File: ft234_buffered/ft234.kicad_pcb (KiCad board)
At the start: 2 copper layers, 17.5 x 10.2 mm, 16 parts, among them J1 USB_OTG, J2 Conn_01x04, U1 FT234XD, U2 74LVC1G17, U3 74LVC1G17

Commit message: migrate to KiCad 7
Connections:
- C1 pad 1: Net-(C1-Pad1) -> (no net)
- C2 pad 1: Net-(C2-Pad1) -> (no net)
- D1 pad 1: Net-(D1-Pad1) -> (no net)
- J1 pad 2: Net-(C1-Pad1) -> Net-(J1-D-)
- J1 pad 3: Net-(C2-Pad1) -> Net-(J1-D+)
- R1 pad 1: Net-(R1-Pad1) -> (no net)
- R1 pad 2: Net-(C1-Pad1) -> Net-(J1-D-)
- R2 pad 1: Net-(R2-Pad1) -> (no net)
- R2 pad 2: Net-(C2-Pad1) -> Net-(J1-D+)
- R4 pad 1: Net-(D1-Pad1) -> Net-(D1-K)
- R4 pad 2: Net-(R4-Pad2) -> (no net)
- U1 pad 1: Net-(R1-Pad1) -> Net-(U1-USBDM)
- U1 pad 10: Net-(U1-Pad10) -> (no net)
- U1 pad 12: Net-(R2-Pad1) -> Net-(U1-UDBDP)
- U1 pad 6: Net-(R4-Pad2) -> Net-(U1-CBUS0)
- U1 pad 7: Net-(U1-Pad7) -> (no net)
- U2 pad 2: Net-(U1-Pad7) -> Net-(U1-TXD)
- U3 pad 4: Net-(U1-Pad10) -> Net-(U1-RXD)
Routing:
- net Net-(U1-TXD): track 0.00 -> 6.06 mm, vias 0 -> 2
- net Net-(U1-Pad7): track 6.06 -> 0.00 mm, vias 2 -> 0
- net Net-(U1-RXD): track 0.00 -> 5.21 mm
- net Net-(U1-Pad10): track 5.21 -> 0.00 mm
- net Net-(J1-D-): track 0.00 -> 4.70 mm
- net Net-(C1-Pad1): track 4.70 -> 0.00 mm
- net Net-(U1-CBUS0): track 0.00 -> 3.44 mm
- net Net-(R4-Pad2): track 3.44 -> 0.00 mm
- net Net-(J1-D+): track 0.00 -> 2.83 mm
- net Net-(C2-Pad1): track 2.83 -> 0.00 mm
- net Net-(D1-Pad1): track 0.99 -> 0.00 mm
- net Net-(D1-K): track 0.00 -> 0.99 mm
- net Net-(U1-UDBDP): track 0.00 -> 0.94 mm
- net Net-(R2-Pad1): track 0.94 -> 0.00 mm
- net Net-(U1-USBDM): track 0.00 -> 0.94 mm
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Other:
- net class Default removed

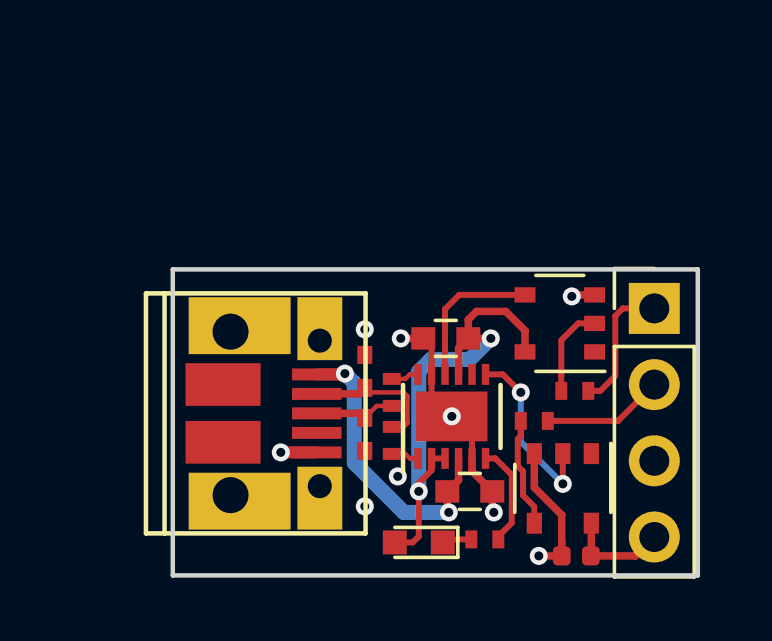
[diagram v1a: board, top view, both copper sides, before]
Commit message: changing buffered ft234 board - wip
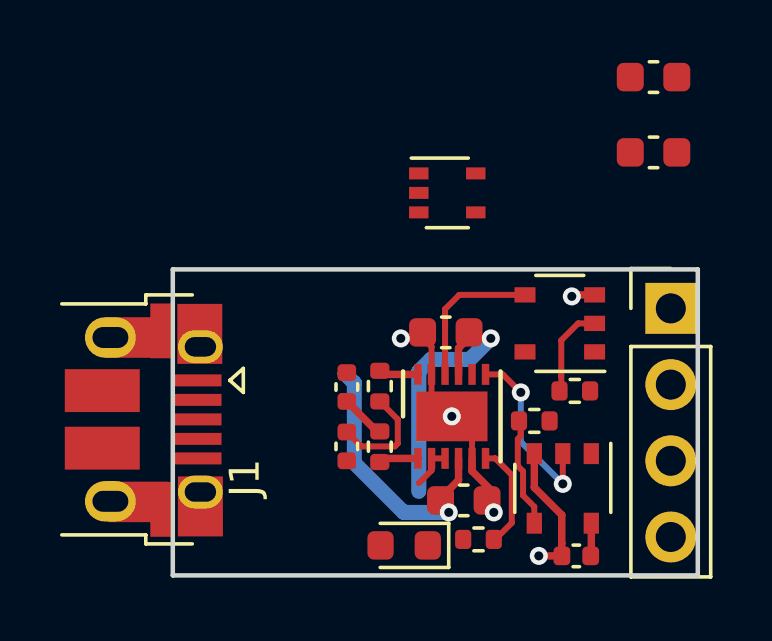
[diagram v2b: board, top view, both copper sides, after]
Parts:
- added C5: 4.7u/6.3V, Capacitor_SMD:C_0603_1608Metric, F.Cu at (156.0, 63.6)
- added C7: 4.7u/6.3V, Capacitor_SMD:C_0603_1608Metric, F.Cu at (156.0, 66.1)
- added U4: MIC5365-2.5YC5, Package_TO_SOT_SMD:SOT-353_SC-70-5, F.Cu at (149.2, 67.5)
- C1, C2: footprint Capacitors_SMD:C_0402_NoSilk -> Capacitor_SMD:C_0402_1005Metric
- C3, C4: footprint Capacitors_SMD:C_0603 -> Capacitor_SMD:C_0603_1608Metric
- D1: footprint LEDs:LED_0603 -> LED_SMD:LED_0603_1608Metric
- J1: footprint hunz:USB_Micro-B_10103594-0001LF -> Connector_USB:USB_Micro-B_Amphenol_10103594-0001LF_Horizontal
- R1, R2, R3, R4, R5: footprint Resistors_SMD:R_0402_NoSilk -> Resistor_SMD:R_0402_1005Metric
- U1: footprint Housings_DFN_QFN:DFN-12-1EP_3x3mm_Pitch0.45mm -> Package_DFN_QFN:DFN-12-1EP_3x3mm_P0.45mm_EP1.66x2.38mm
- moved J1 3.77 mm to (139.0, 75.0), turned to -90 degrees
- moved C1 0.79 mm to (145.8, 73.9)
- moved C2 0.72 mm to (145.8, 75.9)
- moved J2 0.55 mm to (156.6, 71.3)
- moved D1 0.50 mm to (147.7, 79.2)
- moved R1 0.45 mm to (146.9, 75.9)
- moved R2 0.45 mm to (146.9, 73.9)
- moved C4 0.36 mm to (149.7, 77.7)
- moved R4 0.21 mm to (150.2, 79.0)
- moved C3 0.20 mm to (149.1, 72.1)
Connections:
- C1 pad 1: (no net) -> Net-(J1-D-)
- C2 pad 1: (no net) -> Net-(J1-D+)
- D1 pad 1: (no net) -> Net-(D1-K)
- J1 pad 4: (no net) -> unconnected-(J1-ID-Pad4)
- R1 pad 1: (no net) -> Net-(U1-USBDM)
- R2 pad 1: (no net) -> Net-(U1-UDBDP)
- R4 pad 2: (no net) -> Net-(U1-CBUS0)
- U1 pad 10: (no net) -> Net-(U1-RXD)
- U1 pad 7: (no net) -> Net-(U1-TXD)
- U1 pad 8: (no net) -> unconnected-(U1-~{RTS}-Pad8)
- U3 pad 5: +3V3 -> +2V5
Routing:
- net +3V3: track 16.7 -> 10.4 mm, vias 2 -> 1
- net /RXIN: track 4.51 -> 0.00 mm
- net /TXOUT: track 4.05 -> 0.00 mm
- net Net-(J1-D-): track 4.70 -> 1.51 mm
- net /VTG: track 3.47 -> 1.10 mm
- net GND: track 12.7 -> 11.5 mm, vias 9 -> 5
- net Net-(D1-K): track 0.99 -> 0.00 mm
- net +5V: track 9.86 -> 8.92 mm, vias 2 -> 1
- net Net-(J1-D+): track 2.83 -> 3.59 mm

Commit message: foo
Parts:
- moved C7 9.43 mm to (146.7, 67.5), turned to -90 degrees
- moved C5 5.90 mm to (151.6, 67.5), turned to -90 degrees
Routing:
- net GND: track 11.5 -> 10.8 mm, vias 5 -> 4
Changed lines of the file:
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@@
   )
   (footprint "Capacitor_SMD:C_0603_1608Metric" (layer "F.Cu")
-    (at 156.025 63.59)
+    (at 151.6 67.5 -90)
     (descr "Capacitor SMD 0603 (1608 Metric), square (rectangular) end terminal, IPC_7351 nominal, (Body size source: IPC-SM-782 page 76, https://www.pcb-3d.com/wordpress/wp-content/uploads/ipc-sm-782a_amendment_1_and_2.pdf), generated with kicad-footprint-generator")
     (tags "capacitor")
@@
     (property "ki_keywords" "cap capacitor")
     (attr smd)
-    (fp_text reference "C5" (at 0 -1.43) (layer "F.SilkS") hide
+    (fp_text reference "C5" (at 0 -1.43 90) (layer "F.SilkS") hide
         (effects (font (size 1 1) (thickness 0.15)))
     )
-    (fp_text value "4.7u/6.3V" (at 0 1.43) (layer "F.Fab")
+    (fp_text value "4.7u/6.3V" (at 0 1.43 90) (layer "F.Fab")
         (effects (font (size 1 1) (thickness 0.15)))
     )
-    (fp_text user "${REFERENCE}" (at 0 0) (layer "F.Fab")
+    (fp_text user "${REFERENCE}" (at 0 0 90) (layer "F.Fab")
         (effects (font (size 0.4 0.4) (thickness 0.06)))
     )
@@
     (fp_line (start 0.8 0.4) (end -0.8 0.4)
       (stroke (width 0.1) (type solid)) (layer "F.Fab"))
-    (pad "1" smd roundrect (at -0.775 0) (size 0.9 0.95) (layers "F.Cu" "F.Paste" "F.Mask") (roundrect_rratio 0.25)
+    (pad "1" smd roundrect (at -0.775 0 270) (size 0.9 0.95) (layers "F.Cu" "F.Paste" "F.Mask") (roundrect_rratio 0.25)
       (net 19 "+2V5") (pintype "passive"))
-    (pad "2" smd roundrect (at 0.775 0) (size 0.9 0.95) (layers "F.Cu" "F.Paste" "F.Mask") (roundrect_rratio 0.25)
+    (pad "2" smd roundrect (at 0.775 0 270) (size 0.9 0.95) (layers "F.Cu" "F.Paste" "F.Mask") (roundrect_rratio 0.25)
       (net 1 "GND") (pintype "passive"))
     (model "${KICAD6_3DMODEL_DIR}/Capacitor_SMD.3dshapes/C_0603_1608Metric.wrl"
@@
   )
   (footprint "Capacitor_SMD:C_0603_1608Metric" (layer "F.Cu")
-    (at 156.025 66.1)
+    (at 146.7 67.5 -90)
     (descr "Capacitor SMD 0603 (1608 Metric), square (rectangular) end terminal, IPC_7351 nominal, (Body size source: IPC-SM-782 page 76, https://www.pcb-3d.com/wordpress/wp-content/uploads/ipc-sm-782a_amendment_1_and_2.pdf), generated with kicad-footprint-generator")
     (tags "capacitor")
@@
     (property "ki_keywords" "cap capacitor")
     (attr smd)
-    (fp_text reference "C7" (at 0 -1.43) (layer "F.SilkS") hide
+    (fp_text reference "C7" (at 0 -1.43 90) (layer "F.SilkS") hide
         (effects (font (size 1 1) (thickness 0.15)))
     )
-    (fp_text value "4.7u/6.3V" (at 0 1.43) (layer "F.Fab")
+    (fp_text value "4.7u/6.3V" (at 0 1.43 90) (layer "F.Fab")
         (effects (font (size 1 1) (thickness 0.15)))
     )
-    (fp_text user "${REFERENCE}" (at 0 0) (layer "F.Fab")
+    (fp_text user "${REFERENCE}" (at 0 0 90) (layer "F.Fab")
         (effects (font (size 0.4 0.4) (thickness 0.06)))
     )
@@
     (fp_line (start 0.8 0.4) (end -0.8 0.4)
       (stroke (width 0.1) (type solid)) (layer "F.Fab"))
-    (pad "1" smd roundrect (at -0.775 0) (size 0.9 0.95) (layers "F.Cu" "F.Paste" "F.Mask") (roundrect_rratio 0.25)
+    (pad "1" smd roundrect (at -0.775 0 270) (size 0.9 0.95) (layers "F.Cu" "F.Paste" "F.Mask") (roundrect_rratio 0.25)
       (net 5 "+5V") (pintype "passive"))
-    (pad "2" smd roundrect (at 0.775 0) (size 0.9 0.95) (layers "F.Cu" "F.Paste" "F.Mask") (roundrect_rratio 0.25)
+    (pad "2" smd roundrect (at 0.775 0 270) (size 0.9 0.95) (layers "F.Cu" "F.Paste" "F.Mask") (roundrect_rratio 0.25)
       (net 1 "GND") (pintype "passive"))
     (model "${KICAD6_3DMODEL_DIR}/Capacitor_SMD.3dshapes/C_0603_1608Metric.wrl"
@@
   (segment (start 150.65 77.4) (end 150.65 78.05) (width 0.25) (layer "F.Cu") (net 1))
   (segment (start 148.625 74.405) (end 148.705 74.485) (width 0.2) (layer "F.Cu") (net 1))
-  (segment (start 148.35 72.3) (end 147.6 72.3) (width 0.25) (layer "F.Cu") (net 1))
   (segment (start 149.975 76.3) (end 149.975 76.725) (width 0.25) (layer "F.Cu") (net 1))
   (segment (start 152.965 79.55) (end 152.2 79.55) (width 0.25) (layer "F.Cu") (net 1))
@@
   (segment (start 154.06 70.85) (end 153.35 70.85) (width 0.25) (layer "F.Cu") (net 1))
   (via (at 149.3 74.9) (size 0.6) (drill 0.3) (layers "F.Cu" "B.Cu") (net 1))
-  (via (at 147.6 72.3) (size 0.6) (drill 0.3) (layers "F.Cu" "B.Cu") (net 1))
   (via (at 152.2 79.55) (size 0.6) (drill 0.3) (layers "F.Cu" "B.Cu") (net 1))
   (via (at 153.3 70.9) (size 0.6) (drill 0.3) (layers "F.Cu" "B.Cu") (net 1))

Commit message: wip
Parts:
- C3, C4, C5, C7: footprint Capacitor_SMD:C_0603_1608Metric -> Capacitor_SMD:C_0402_1005Metric
- moved U4 4.83 mm to (146.4, 71.5)
- moved C7 4.39 mm to (143.8, 70.8), turned to 180 degrees
- moved C5 4.06 mm to (149.1, 70.7), turned to 0 degrees
- moved J1 2.90 mm to (141.8, 75.8)
- moved D1 0.95 mm to (147.2, 78.4), turned to 90 degrees
- moved C4 0.20 mm to (149.7, 77.5)
- moved C3 0.20 mm to (149.1, 72.3)
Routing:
- net GND: track 10.8 -> 24.7 mm, vias 4 -> 12
- net +5V: track 8.92 -> 19.3 mm, vias 1 -> 2
- net +2V5: track 0.00 -> 8.54 mm
- net Net-(J1-D-): track 1.51 -> 4.00 mm
- net Net-(J1-D+): track 3.59 -> 5.93 mm
- net Net-(U1-TXD): track 6.06 -> 4.37 mm, vias 2 -> 0
- net Net-(U1-RXD): track 5.21 -> 4.63 mm
- net +3V3: track 10.4 -> 10.7 mm, vias 1 -> 2
- removed copper zone on F.Cu, net GND
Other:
- board size 17.5 x 10.2 mm -> 18.7 x 10.2 mm

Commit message: done
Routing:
- net GND: track 24.7 -> 33.2 mm, vias 12 -> 13
- net /TXOUT: track 0.00 -> 4.54 mm
- net /RXIN: track 0.00 -> 4.36 mm
- net +5V: track 19.3 -> 22.7 mm
- net /VTG: track 1.10 -> 4.03 mm
- net Net-(D1-K): track 0.00 -> 2.56 mm
- net Net-(U1-CBUS0): track 3.44 -> 2.90 mm
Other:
- board size 18.7 x 10.2 mm -> 19.1 x 10.5 mm
- board text added: "v2"
- board text added: "znu2023"
- board text removed: "v1"
- board text removed: "znu19"

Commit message: add fiducials
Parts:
- added FID1: Fiducial, Fiducial:Fiducial_0.5mm_Mask1mm, F.Cu at (139.5, 70.5)
- added FID2: Fiducial, Fiducial:Fiducial_0.5mm_Mask1mm, F.Cu at (139.5, 79.6)
- added FID3: Fiducial, Fiducial:Fiducial_0.5mm_Mask1mm, F.Cu at (155.2, 77.6)
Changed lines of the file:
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@@
     )
+  )
+  (footprint "Fiducial:Fiducial_0.5mm_Mask1mm" (layer "F.Cu")
+    (at 139.5 70.5)
+    (descr "Circular Fiducial, 0.5mm bare copper, 1mm soldermask opening (Level C)")
+    (tags "fiducial")
+    (property "Sheetfile" "ft234.kicad_sch")
+    (property "Sheetname" "")
+    (property "ki_description" "Fiducial Marker")
+    (property "ki_keywords" "fiducial marker")
+    (attr smd)
+    (fp_text reference "FID1" (at 0 -1.5) (layer "F.SilkS") hide
+        (effects (font (size 1 1) (thickness 0.15)))
+    )
+    (fp_text value "Fiducial" (at 0 1.5) (layer "F.Fab")
+        (effects (font (size 1 1) (thickness 0.15)))
+    )
+    (fp_text user "${REFERENCE}" (at 0 0) (layer "F.Fab")
+        (effects (font (size 0.2 0.2) (thickness 0.04)))
+    )
+    (fp_circle (center 0 0) (end 0.75 0)
+      (stroke (width 0.05) (type solid)) (fill none) (layer "F.CrtYd"))
+    (fp_circle (center 0 0) (end 0.5 0)
+      (stroke (width 0.1) (type solid)) (fill none) (layer "F.Fab"))
+    (pad "" smd circle (at 0 0) (size 0.5 0.5) (layers "F.Cu" "F.Mask")
+      (solder_mask_margin 0.25) (clearance 0.25))
   )
   (footprint "Capacitor_SMD:C_0402_1005Metric" (layer "F.Cu")
@@
     )
   )
+  (footprint "Fiducial:Fiducial_0.5mm_Mask1mm" (layer "F.Cu")
+    (at 139.5 79.6)
+    (descr "Circular Fiducial, 0.5mm bare copper, 1mm soldermask opening (Level C)")
+    (tags "fiducial")
+    (property "Sheetfile" "ft234.kicad_sch")
+    (property "Sheetname" "")
+    (property "ki_description" "Fiducial Marker")
+    (property "ki_keywords" "fiducial marker")
+    (attr smd)
+    (fp_text reference "FID2" (at 0 -1.5) (layer "F.SilkS") hide
+        (effects (font (size 1 1) (thickness 0.15)))
+    )
+    (fp_text value "Fiducial" (at 0 1.5) (layer "F.Fab")
+        (effects (font (size 1 1) (thickness 0.15)))
+    )
+    (fp_text user "${REFERENCE}" (at 0 0) (layer "F.Fab")
+        (effects (font (size 0.2 0.2) (thickness 0.04)))
+    )
+    (fp_circle (center 0 0) (end 0.75 0)
+      (stroke (width 0.05) (type solid)) (fill none) (layer "F.CrtYd"))
+    (fp_circle (center 0 0) (end 0.5 0)
+      (stroke (width 0.1) (type solid)) (fill none) (layer "F.Fab"))
+    (pad "" smd circle (at 0 0) (size 0.5 0.5) (layers "F.Cu" "F.Mask")
+      (solder_mask_margin 0.25) (clearance 0.25))
+  )
+  (footprint "Fiducial:Fiducial_0.5mm_Mask1mm" (layer "F.Cu")
+    (at 155.2 77.6)
+    (descr "Circular Fiducial, 0.5mm bare copper, 1mm soldermask opening (Level C)")
+    (tags "fiducial")
+    (property "Sheetfile" "ft234.kicad_sch")
+    (property "Sheetname" "")
+    (property "ki_description" "Fiducial Marker")
+    (property "ki_keywords" "fiducial marker")
+    (attr smd)
+    (fp_text reference "FID3" (at 0 -1.5) (layer "F.SilkS") hide
+        (effects (font (size 1 1) (thickness 0.15)))
+    )
+    (fp_text value "Fiducial" (at 0 1.5) (layer "F.Fab")
+        (effects (font (size 1 1) (thickness 0.15)))
+    )
+    (fp_text user "${REFERENCE}" (at 0 0) (layer "F.Fab")
+        (effects (font (size 0.2 0.2) (thickness 0.04)))
+    )
+    (fp_circle (center 0 0) (end 0.75 0)
+      (stroke (width 0.05) (type solid)) (fill none) (layer "F.CrtYd"))
+    (fp_circle (center 0 0) (end 0.5 0)
+      (stroke (width 0.1) (type solid)) (fill none) (layer "F.Fab"))
+    (pad "" smd circle (at 0 0) (size 0.5 0.5) (layers "F.Cu" "F.Mask")
+      (solder_mask_margin 0.25) (clearance 0.25))
+  )
   (footprint "Capacitor_SMD:C_0402_1005Metric" (layer "F.Cu")
